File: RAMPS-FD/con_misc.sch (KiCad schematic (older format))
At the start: 15 parts, among them K201 SER1, K202 SER2, K203 SER3, K204 SER4, P1 SERIAL1, P2 I2C-1, P211 I2C-0, P213 AUX-4, P214 AUX-2, P215 AUX-3, P216 SERIAL0

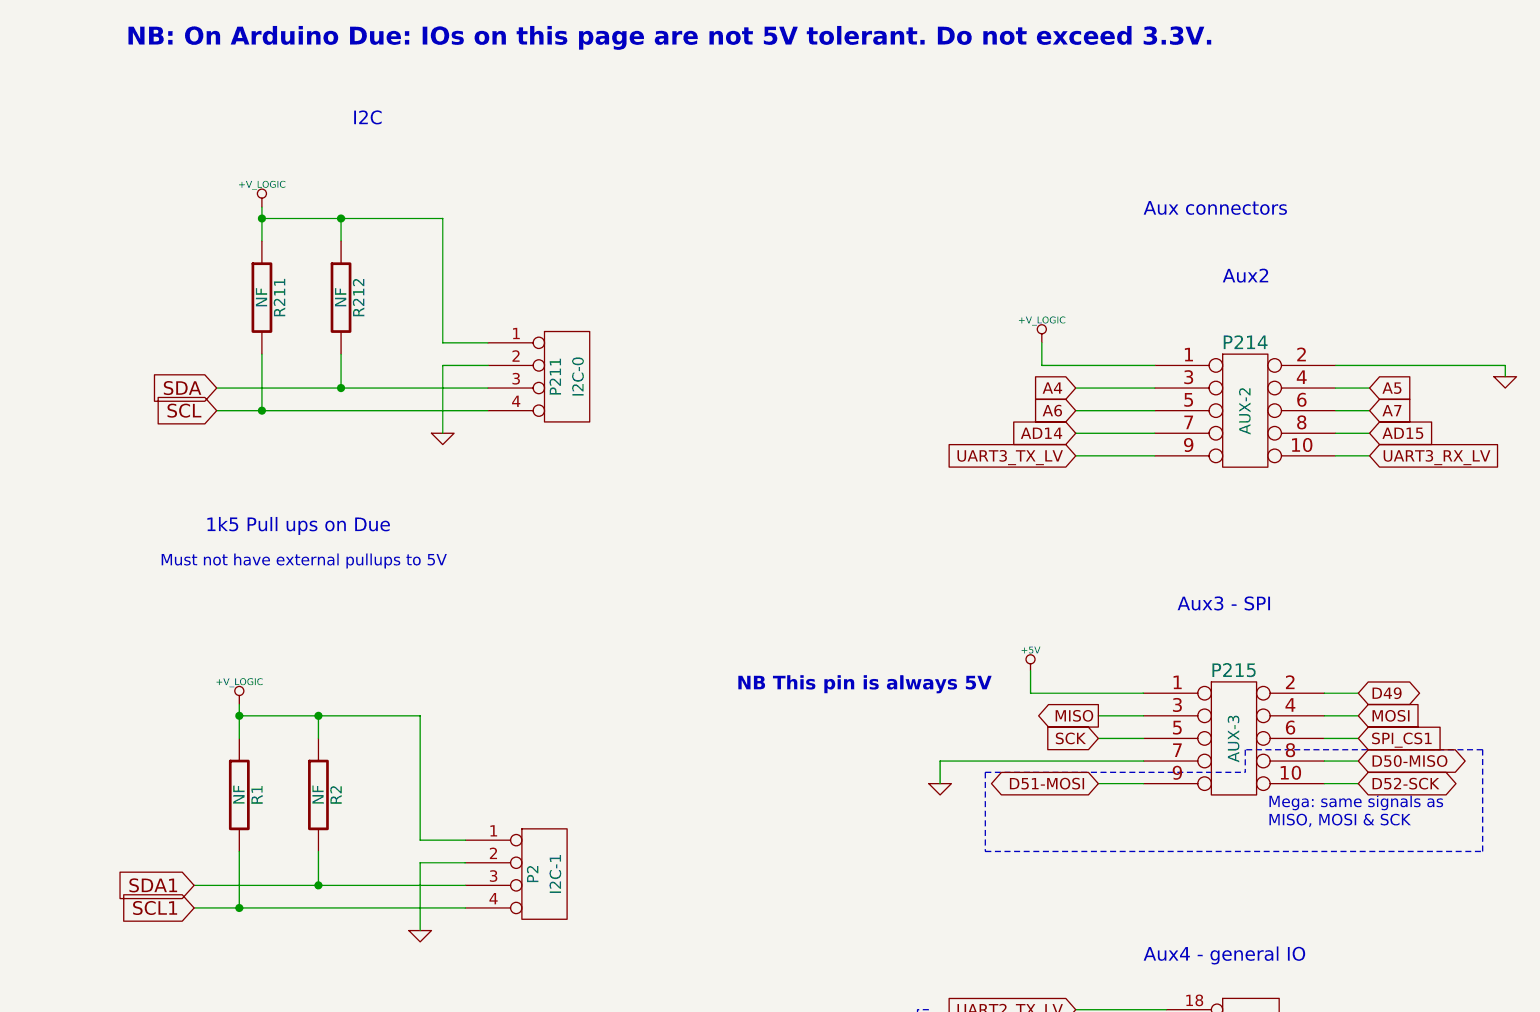
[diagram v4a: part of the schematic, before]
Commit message: RAMPS-FD: update schematic, layout
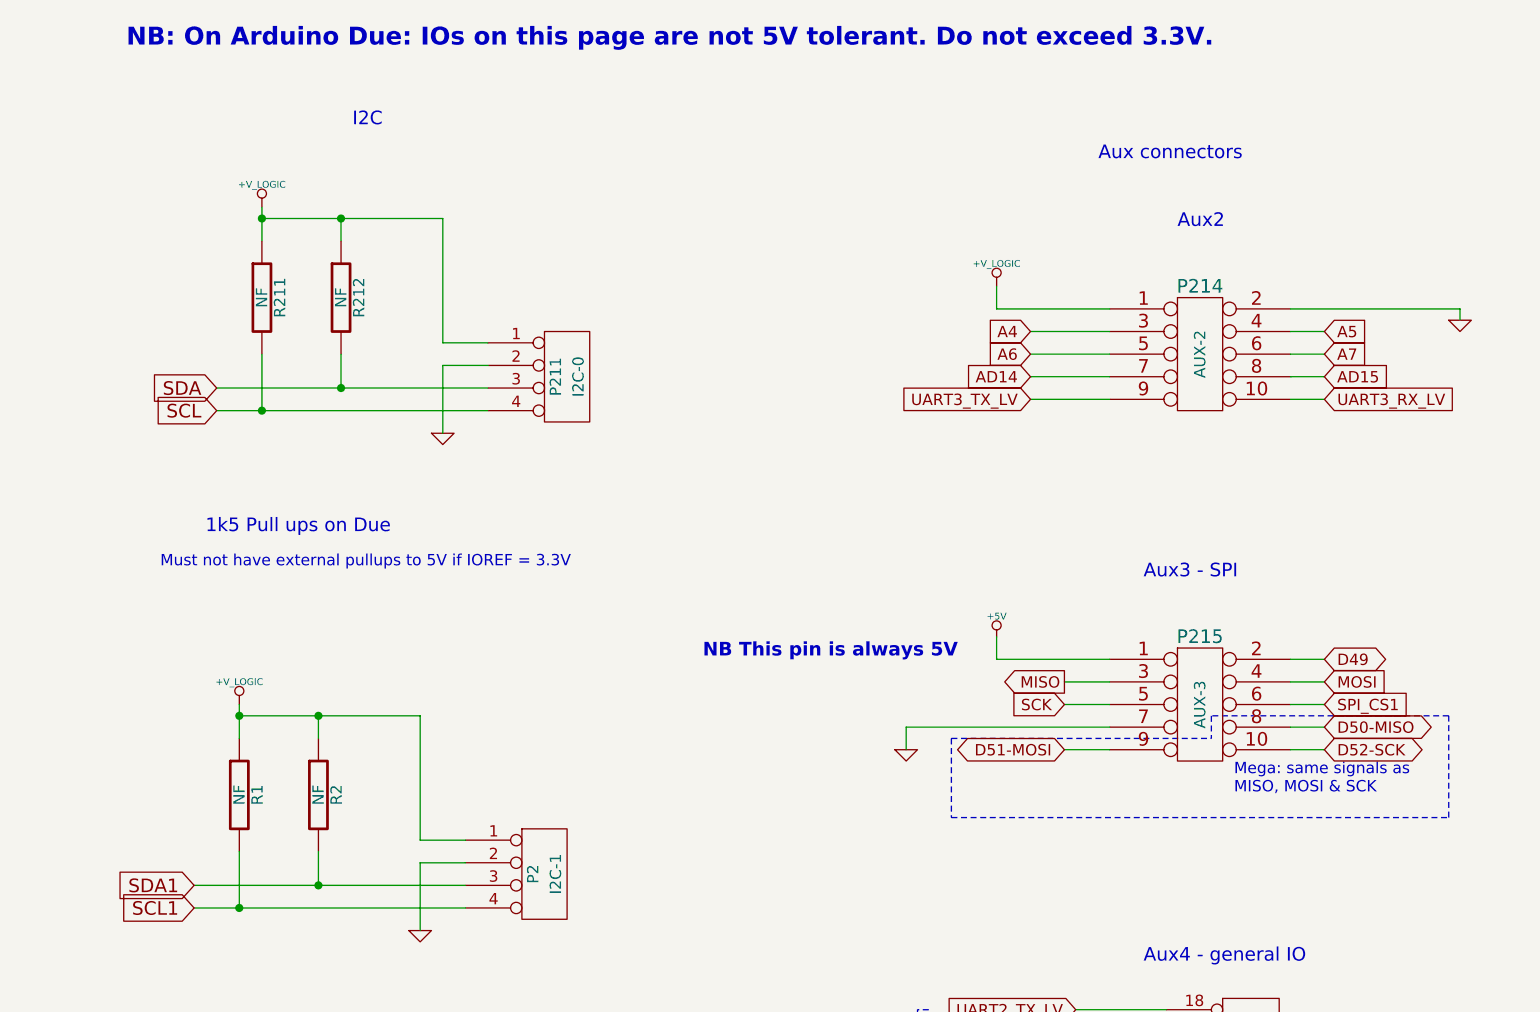
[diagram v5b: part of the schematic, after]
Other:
- note added: "Must not have external pullups to 5V if IOREF = 3.3V"
- note removed: "Must not have external pullups to 5V"
- moved on the sheet: P214, P215
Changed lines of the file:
@@
 Sheet 6 9
 Title ""
-Date "24 sep 2013"
+Date "26 sep 2013"
 Rev "0.2"
 Comp ""
@@
 Comment4 ""
 $EndDescr
-Text GLabel 9600 2600 2    50   Input ~ 0
+Text GLabel 9400 2350 2    50   Input ~ 0
 AD15
-Text GLabel 8300 2600 0    50   Input ~ 0
+Text GLabel 8100 2350 0    50   Input ~ 0
 AD14
 Wire Wire Line
-	9550 4150 9400 4150
+	9400 4000 9250 4000
 Wire Wire Line
 	1950 2350 1950 1550
@@
 	8450 6750 8700 6750
 Wire Wire Line
-	8400 3950 8600 3950
-Wire Wire Line
-	9550 3850 9400 3850
-Wire Wire Line
-	9550 4050 9400 4050
-Wire Wire Line
-	9600 2600 9450 2600
-Wire Wire Line
-	9600 2400 9450 2400
-Wire Wire Line
-	8650 2600 8300 2600
-Wire Wire Line
-	8300 2400 8650 2400
-Wire Wire Line
-	7700 4150 7700 4050
-Wire Wire Line
-	8600 3750 8100 3750
-Wire Wire Line
-	8100 3750 8100 3650
-Wire Wire Line
-	9450 2300 10200 2300
+	8250 3800 8450 3800
+Wire Wire Line
+	9400 3700 9250 3700
+Wire Wire Line
+	9400 3900 9250 3900
+Wire Wire Line
+	9400 2350 9250 2350
+Wire Wire Line
+	9400 2150 9250 2150
+Wire Wire Line
+	8450 2350 8100 2350
+Wire Wire Line
+	8100 2150 8450 2150
+Wire Wire Line
+	7550 4000 7550 3900
+Wire Wire Line
+	8450 3600 7950 3600
+Wire Wire Line
+	7950 3600 7950 3500
+Wire Wire Line
+	9250 2050 10000 2050
 Wire Wire Line
 	2450 1850 1850 1850
@@
 	1850 1950 2450 1950
 Wire Wire Line
-	8150 2200 8150 2300
-Wire Wire Line
-	8150 2300 8650 2300
-Wire Wire Line
-	10200 2300 10200 2350
-Wire Wire Line
-	8300 2500 8650 2500
-Wire Wire Line
-	8300 2700 8650 2700
-Wire Wire Line
-	9450 2500 9600 2500
-Wire Wire Line
-	9450 2700 9600 2700
-Wire Wire Line
-	9400 3950 9550 3950
-Wire Wire Line
-	8600 3850 8400 3850
+	7950 1950 7950 2050
+Wire Wire Line
+	7950 2050 8450 2050
+Wire Wire Line
+	10000 2050 10000 2100
+Wire Wire Line
+	8100 2250 8450 2250
+Wire Wire Line
+	8100 2450 8450 2450
+Wire Wire Line
+	9250 2250 9400 2250
+Wire Wire Line
+	9250 2450 9400 2450
+Wire Wire Line
+	9250 3800 9400 3800
+Wire Wire Line
+	8450 3700 8250 3700
 Wire Wire Line
 	8300 5150 8700 5150
@@
 	4950 4450 4950 4600
 Connection ~ 4950 4600
-Text GLabel 9550 4050 2    50   BiDi ~ 0
+Text GLabel 9400 3900 2    50   BiDi ~ 0
 D50-MISO
-Text GLabel 9550 4150 2    50   BiDi ~ 0
+Text GLabel 9400 4000 2    50   BiDi ~ 0
 D52-SCK
 $Comp
@@
 L CONN_5X2 P215
 U 1 1 523A2434
-P 9000 3950
-F 0 "P215" H 9000 4250 60  0000 C CNN
-F 1 "AUX-3" V 9000 3950 50  0000 C CNN
-F 2 "" H 9000 3950 60  0001 C CNN
-F 3 "" H 9000 3950 60  0001 C CNN
-	1    9000 3950
+P 8850 3800
+F 0 "P215" H 8850 4100 60  0000 C CNN
+F 1 "AUX-3" V 8850 3800 50  0000 C CNN
+F 2 "" H 8850 3800 60  0001 C CNN
+F 3 "" H 8850 3800 60  0001 C CNN
+	1    8850 3800
 	1    0    0    -1
 $EndComp
@@
 Text Notes 550  1950 0    50   ~ 0
 UART-TTL
-Text GLabel 8300 2500 0    50   Input ~ 0
+Text GLabel 8100 2250 0    50   Input ~ 0
 A6
-Text GLabel 9600 2500 2    50   Input ~ 0
+Text GLabel 9400 2250 2    50   Input ~ 0
 A7
-Text GLabel 9600 2400 2    50   Input ~ 0
+Text GLabel 9400 2150 2    50   Input ~ 0
 A5
-Text GLabel 8300 2400 0    50   Input ~ 0
+Text GLabel 8100 2150 0    50   Input ~ 0
 A4
-Text GLabel 8400 4150 0    50   BiDi ~ 0
+Text GLabel 8250 4000 0    50   BiDi ~ 0
 D51-MOSI
 $Comp
 L +V_LOGIC #PWR071
 U 1 1 517867DD
-P 8150 2200
-F 0 "#PWR071" H 8150 2170 30  0001 C CNN
-F 1 "+V_LOGIC" H 8150 2300 30  0000 C CNN
-F 2 "" H 8150 2200 60  0001 C CNN
-F 3 "" H 8150 2200 60  0001 C CNN
-	1    8150 2200
+P 7950 1950
+F 0 "#PWR071" H 7950 1920 30  0001 C CNN
+F 1 "+V_LOGIC" H 7950 2050 30  0000 C CNN
+F 2 "" H 7950 1950 60  0001 C CNN
+F 3 "" H 7950 1950 60  0001 C CNN
+	1    7950 1950
 	1    0    0    -1
 $EndComp
@@
 	1    0    0    1
 $EndComp
-Text GLabel 9550 3750 2    50   BiDi ~ 0
+Text GLabel 9400 3600 2    50   BiDi ~ 0
 D49
-Text GLabel 9550 3850 2    50   Input ~ 0
+Text GLabel 9400 3700 2    50   Input ~ 0
 MOSI
-Text GLabel 8400 3950 0    50   Input ~ 0
+Text GLabel 8250 3800 0    50   Input ~ 0
 SCK
-Text GLabel 8400 3850 0    50   Output ~ 0
+Text GLabel 8250 3700 0    50   Output ~ 0
 MISO
 Text Notes 2200 7450 2    50   ~ 0
 Need buffered outputs?
 Text Notes 4250 3200 0    50   ~ 0
-Must not have external pullups to 5V
+Must not have external pullups to 5V if IOREF = 3.3V
 $Comp
 L GND #PWR075
 U 1 1 5104884C
-P 7700 4150
-F 0 "#PWR075" H 7700 4150 30  0001 C CNN
-F 1 "GND" H 7700 4080 30  0001 C CNN
-F 2 "" H 7700 4150 60  0001 C CNN
-F 3 "" H 7700 4150 60  0001 C CNN
-	1    7700 4150
+P 7550 4000
+F 0 "#PWR075" H 7550 4000 30  0001 C CNN
+F 1 "GND" H 7550 3930 30  0001 C CNN
+F 2 "" H 7550 4000 60  0001 C CNN
+F 3 "" H 7550 4000 60  0001 C CNN
+	1    7550 4000
 	1    0    0    -1
 $EndComp
@@
 L GND #PWR076
 U 1 1 51048839
-P 10200 2350
-F 0 "#PWR076" H 10200 2350 30  0001 C CNN
-F 1 "GND" H 10200 2280 30  0001 C CNN
-F 2 "" H 10200 2350 60  0001 C CNN
-F 3 "" H 10200 2350 60  0001 C CNN
-	1    10200 2350
+P 10000 2100
+F 0 "#PWR076" H 10000 2100 30  0001 C CNN
+F 1 "GND" H 10000 2030 30  0001 C CNN
+F 2 "" H 10000 2100 60  0001 C CNN
+F 3 "" H 10000 2100 60  0001 C CNN
+	1    10000 2100
 	1    0    0    -1
 $EndComp
@@
 Text Notes 8600 4950 0    60   ~ 0
 Aux4 - general IO
-Text Notes 8750 3400 0    60   ~ 0
+Text Notes 8600 3250 0    60   ~ 0
 Aux3 - SPI
-Text Notes 8950 1950 0    60   ~ 0
+Text Notes 8750 1700 0    60   ~ 0
 Aux2
-Text Notes 8600 1650 0    60   ~ 0
+Text Notes 8400 1400 0    60   ~ 0
 Aux connectors
 Text Notes 1350 7300 0    60   ~ 0
@@
 L CONN_5X2 P214
 U 1 1 510481EC
-P 9050 2500
-F 0 "P214" H 9050 2800 60  0000 C CNN
-F 1 "AUX-2" V 9050 2500 50  0000 C CNN
-F 2 "" H 9050 2500 60  0001 C CNN
-F 3 "" H 9050 2500 60  0001 C CNN
-	1    9050 2500
+P 8850 2250
+F 0 "P214" H 8850 2550 60  0000 C CNN
+F 1 "AUX-2" V 8850 2250 50  0000 C CNN
+F 2 "" H 8850 2250 60  0001 C CNN
+F 3 "" H 8850 2250 60  0001 C CNN
+	1    8850 2250
 	1    0    0    -1
 $EndComp
@@
 Text Notes 550  1600 0    50   ~ 0
 Note: this serial port is shared with\nUSB programming port
-Text GLabel 9550 3950 2    50   Input ~ 0
+Text GLabel 9400 3800 2    50   Input ~ 0
 SPI_CS1
 Wire Wire Line
-	8400 4150 8600 4150
-Wire Wire Line
-	7700 4050 8600 4050
+	8250 4000 8450 4000
+Wire Wire Line
+	7550 3900 8450 3900
 Wire Notes Line
 	7600 6150 7600 6650
@@
 Text GLabel 8300 5150 0    50   Input ~ 0
 UART2_TX_LV
-Text GLabel 8300 2700 0    50   Input ~ 0
+Text GLabel 8100 2450 0    50   Input ~ 0
 UART3_TX_LV
-Text GLabel 9600 2700 2    50   Input ~ 0
+Text GLabel 9400 2450 2    50   Input ~ 0
 UART3_RX_LV
 Text Notes 6550 6400 0    50   ~ 0
 These are shared with E1 \nand E2 stepper signals
-Text Notes 9150 4350 0    50   ~ 0
+Text Notes 9000 4200 0    50   ~ 0
 Mega: same signals as \nMISO, MOSI & SCK
 Wire Wire Line
-	9550 3750 9400 3750
+	9400 3600 9250 3600
 Text GLabel 8300 6650 0    50   BiDi ~ 0
 D32
@@
 L +5V #PWR087
 U 1 1 52421C84
-P 8100 3650
-F 0 "#PWR087" H 8100 3740 20  0001 C CNN
-F 1 "+5V" H 8100 3740 30  0000 C CNN
-F 2 "" H 8100 3650 60  0000 C CNN
-F 3 "" H 8100 3650 60  0000 C CNN
-	1    8100 3650
-	1    0    0    -1
-$EndComp
-Text Notes 6800 3750 0    60   ~ 12
+P 7950 3500
+F 0 "#PWR087" H 7950 3590 20  0001 C CNN
+F 1 "+5V" H 7950 3590 30  0000 C CNN
+F 2 "" H 7950 3500 60  0000 C CNN
+F 3 "" H 7950 3500 60  0000 C CNN
+	1    7950 3500
+	1    0    0    -1
+$EndComp
+Text Notes 6650 3600 0    60   ~ 12
 NB This pin is always 5V
 Wire Notes Line
@@
 	7600 6650 7650 6650
 Wire Notes Line
-	7900 4100 9050 4100
-Wire Notes Line
-	7900 4100 7900 4450
-Wire Notes Line
-	7900 4450 10100 4450
-Wire Notes Line
-	10100 4450 10100 4000
-Wire Notes Line
-	10100 4000 9050 4000
-Wire Notes Line
-	9050 4000 9050 4100
+	7750 3950 8900 3950
+Wire Notes Line
+	7750 3950 7750 4300
+Wire Notes Line
+	7750 4300 9950 4300
+Wire Notes Line
+	9950 4300 9950 3850
+Wire Notes Line
+	9950 3850 8900 3850
+Wire Notes Line
+	8900 3850 8900 3950
 $EndSCHEMATC

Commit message: RAMPS-FD: version 1 Rev A
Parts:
- removed P215: AUX-3, symbol CONN_5X2
- added P215: AUX-3, symbol CONN_6X2
- K201: value SER1 -> S1
- K202: value SER2 -> S2
- K203: value SER3 -> S3
- K204: value SER4 -> S4
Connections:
- net +5V: now also P215.1 (P1)
- net +V_LOGIC: now also P215.12
- net D49: now also P215.2 (P2)
- net D50-MISO: now also P215.9
- net D51-MOSI: now also P215.10
- net D52-SCK: now also P215.11
- net GND: now also P215.7 (P7)
- net MISO: now also P215.3 (P3)
- net MOSI: now also P215.4 (P4)
- net SCK: now also P215.5 (P5)
- net SPI_CS1: now also P215.6 (P6)
- no-connect marks 6 -> 7
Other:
- note added: "Note: Some addon boards \nconnect this pin to GND."
- moved on the sheet: P2, P211, P213, P214, R1, R2, R211, R212
